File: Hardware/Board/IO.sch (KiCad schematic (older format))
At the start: 70 parts, among them U1 PCF8574A, U2 PCF8574A, U3 TJA1029T, U4 TJA1029T, U5 TJA1029T, U6 TJA1049T-3, U7 MAX3072E

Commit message: MCU Section fertig, Analog Inputs angelegt, Schaltplan neu organisiert, alte Datenblätter entfernt.
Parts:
- removed U?: MAX11613, Package_SO:MSOP-8_3x3mm_P0.65mm, symbol Analog_ADC:MAX11613
- added U?: MAX11615, Package_SO:QSOP-16_3.9x4.9mm_P0.635mm, symbol Analog_ADC:MAX11615
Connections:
- net labels added: AIN4, AIN5, AIN6, AIN7, P0, P1, P2, P3, P4, P5, P6, P7
- net labels removed: I2C1_SCL, I2C1_SDA
- wire segments 273 -> 277
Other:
- note added: "I2C ADR: 0011000"
- note added: "I2C-ADR: 0110011"
- note removed: "I2C-ADR: 0110100"
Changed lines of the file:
@@
 $Descr A3 16535 11693
 encoding utf-8
-Sheet 2 7
+Sheet 2 6
 Title ""
 Date ""
@@
 Wire Wire Line
 	13000 5100 12850 5100
-Text GLabel 11750 7500 0    50   BiDi ~ 0
+Text GLabel 11750 7900 0    50   BiDi ~ 0
 I2C2_SDA
-Text GLabel 11750 7400 0    50   Input ~ 0
+Text GLabel 11750 7800 0    50   Input ~ 0
 I2C2_SCL
 Wire Wire Line
@@
 Wire Wire Line
 	11850 4400 11750 4400
-$Comp
-L Analog_ADC:MAX11613 U?
-U 1 1 5D89986D
-P 12350 7500
-F 0 "U?" H 12800 8000 50  0000 C CNN
-F 1 "MAX11613" H 12700 7900 50  0000 C CNN
-F 2 "Package_SO:MSOP-8_3x3mm_P0.65mm" H 12800 7150 50  0001 L CNN
-F 3 "https://datasheets.maximintegrated.com/en/ds/MAX11612-MAX11617.pdf" H 12450 8000 50  0001 C CNN
-	1    12350 7500
-	-1   0    0    -1
-$EndComp
 $Comp
 L power:GND #PWR?
@@
 	0    1    1    0
 $EndComp
-$Comp
-L power:GND #PWR?
-U 1 1 5D8DBE2A
-P 12350 8100
-F 0 "#PWR?" H 12350 7850 50  0001 C CNN
-F 1 "GND" H 12355 7927 50  0000 C CNN
-F 2 "" H 12350 8100 50  0001 C CNN
-F 3 "" H 12350 8100 50  0001 C CNN
-	1    12350 8100
-	1    0    0    -1
-$EndComp
 Wire Wire Line
 	12350 6750 12350 6850
@@
 Wire Wire Line
 	12350 6850 12350 7100
-Wire Wire Line
-	11850 7400 11750 7400
-Wire Wire Line
-	11850 7500 11750 7500
-Wire Wire Line
-	12350 8000 12350 8100
-Text Notes 11450 8050 0    50   ~ 0
-I2C-ADR: 0110100
+Text Notes 11450 8650 0    50   ~ 0
+I2C-ADR: 0110011
 Text Notes 11500 3050 0    50   ~ 0
 I2C ADR: 0111001
@@
 $EndComp
 Text GLabel 6000 8150 2    50   BiDi ~ 0
-I2C1_SDA
+I2C2_SDA
 Text GLabel 6000 9150 2    50   Input ~ 0
-I2C1_SCL
+I2C2_SCL
 $Comp
 L power:+3.3VA #PWR?
@@
 Wire Wire Line
 	9750 8250 9550 8250
+Text Notes 4650 9650 0    50   ~ 0
+I2C ADR: 0011000
+$Comp
+L Analog_ADC:MAX11615 U?
+U 1 1 5F61F3FA
+P 12350 7800
+F 0 "U?" H 12750 8600 50  0000 C CNN
+F 1 "MAX11615" H 12700 8500 50  0000 C CNN
+F 2 "Package_SO:QSOP-16_3.9x4.9mm_P0.635mm" H 12800 7150 50  0001 L CNN
+F 3 "https://datasheets.maximintegrated.com/en/ds/MAX11612-MAX11617.pdf" H 12450 8600 50  0001 C CNN
+	1    12350 7800
+	-1   0    0    -1
+$EndComp
+Text GLabel 12950 7700 2    50   Input ~ 0
+AIN4
+Text GLabel 12950 7800 2    50   Input ~ 0
+AIN5
+Text GLabel 12950 7900 2    50   Input ~ 0
+AIN6
+Text GLabel 12950 8000 2    50   Input ~ 0
+AIN7
+Wire Wire Line
+	11750 7800 11850 7800
+Wire Wire Line
+	11850 7900 11750 7900
+Wire Wire Line
+	12950 7700 12850 7700
+Wire Wire Line
+	12950 7800 12850 7800
+Wire Wire Line
+	12950 7900 12850 7900
+Wire Wire Line
+	12950 8000 12850 8000
+$Comp
+L power:GND #PWR?
+U 1 1 5F70EB36
+P 12350 8700
+F 0 "#PWR?" H 12350 8450 50  0001 C CNN
+F 1 "GND" H 12355 8527 50  0000 C CNN
+F 2 "" H 12350 8700 50  0001 C CNN
+F 3 "" H 12350 8700 50  0001 C CNN
+	1    12350 8700
+	1    0    0    -1
+$EndComp
+Wire Wire Line
+	12350 8600 12350 8700
+Text GLabel 13000 4400 2    50   BiDi ~ 0
+P0
+Text GLabel 13000 4500 2    50   BiDi ~ 0
+P1
+Text GLabel 13000 4600 2    50   BiDi ~ 0
+P2
+Text GLabel 13000 4700 2    50   BiDi ~ 0
+P3
+Text GLabel 13000 4800 2    50   BiDi ~ 0
+P4
+Text GLabel 13000 4900 2    50   BiDi ~ 0
+P5
+Text GLabel 13000 5000 2    50   BiDi ~ 0
+P6
+Text GLabel 13000 5100 2    50   BiDi ~ 0
+P7
 $EndSCHEMATC

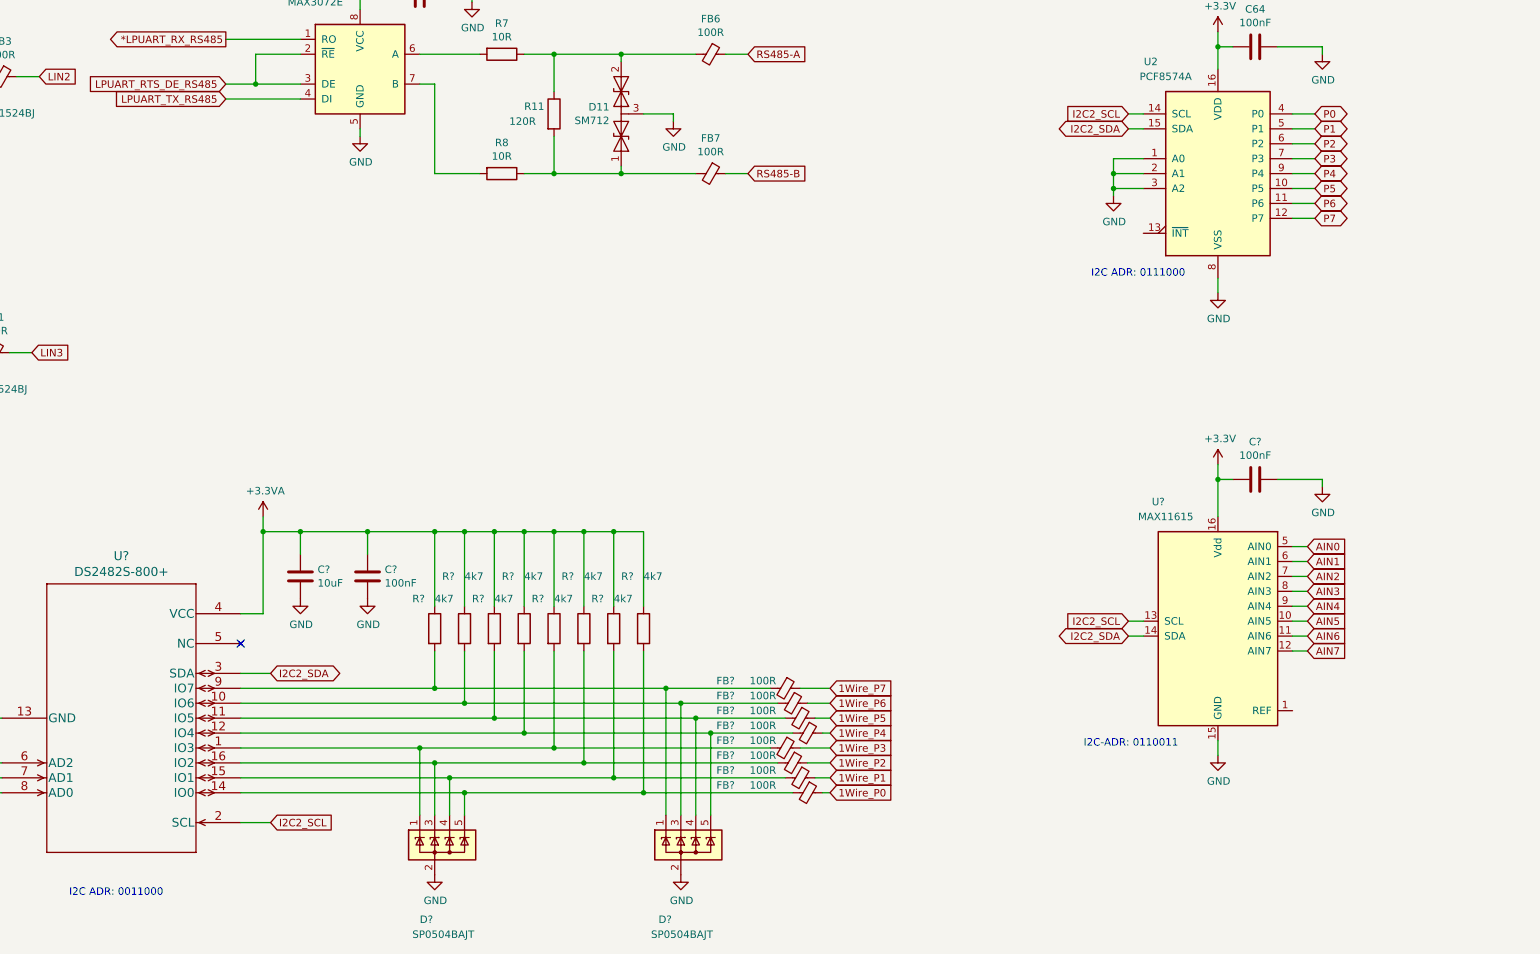
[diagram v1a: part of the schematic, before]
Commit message: Trennung MCU und Rest, Footprints fast alles zugewiesen, GSM Modul integriert, viel Kleinkram
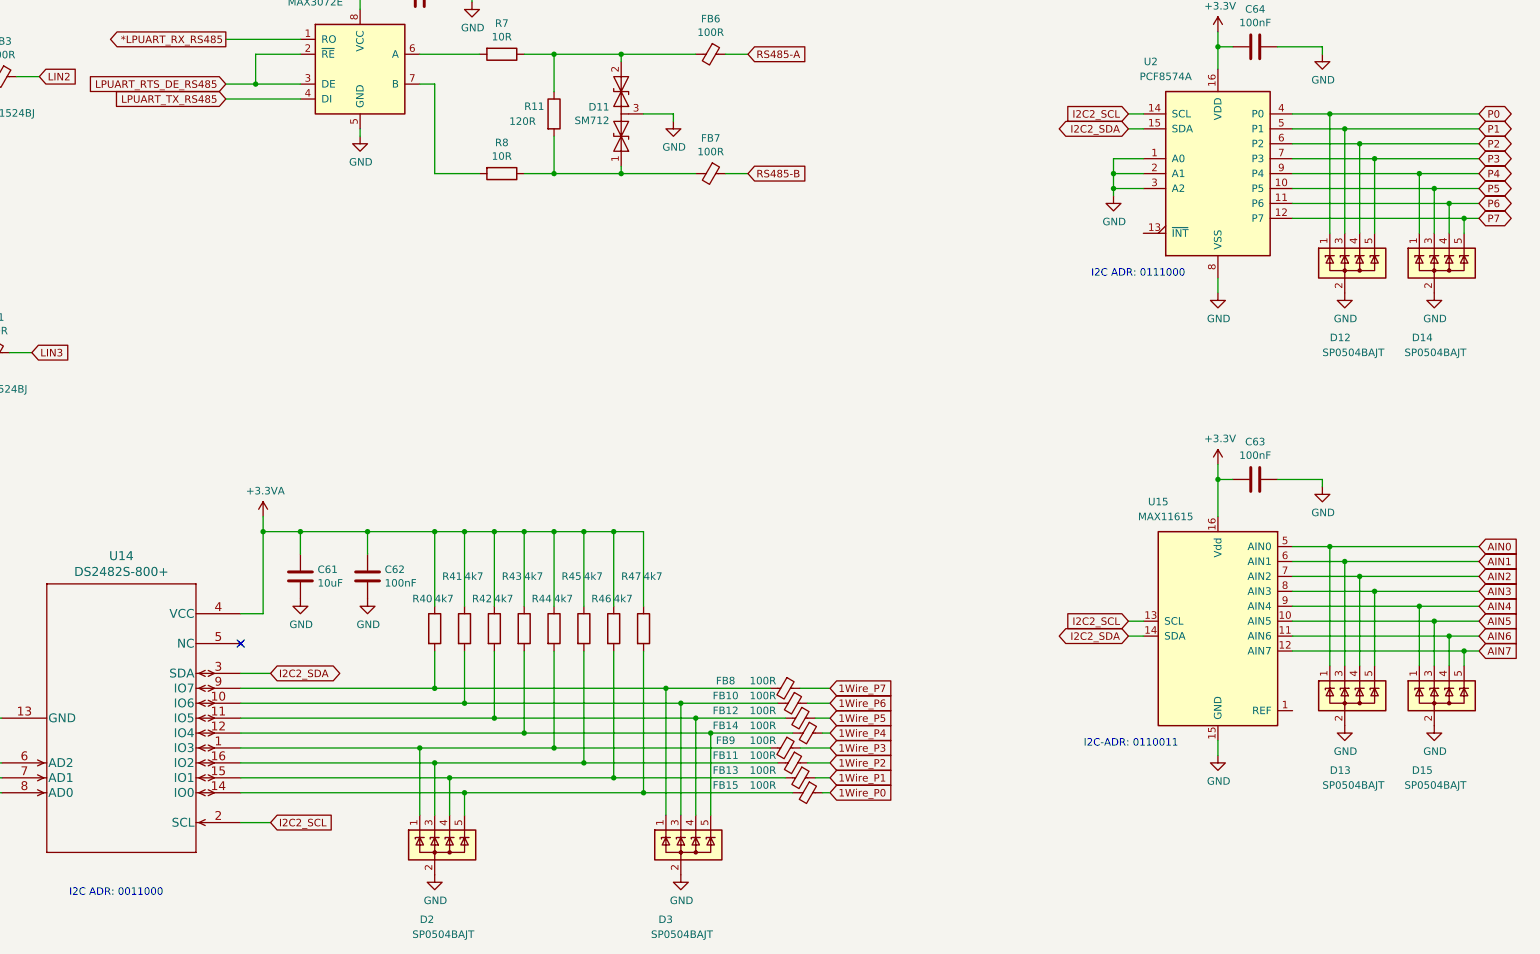
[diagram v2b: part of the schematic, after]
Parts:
- added D12, D13, D14, D15: SP0504BAJT, Package_TO_SOT_SMD:SOT-353_SC-70-5, symbol Power_Protection:SP0504BAJT
- U1, U2: footprint (none) -> Package_SO:SOIC-16W_7.5x10.3mm_P1.27mm
- gave numbers to parts that had none: 23
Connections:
- net AIN0: now also D13.1 (K)
- net AIN1: now also D13.3 (K)
- net AIN2: now also D13.4 (K)
- net AIN3: now also D13.5 (K)
- net AIN4: now also D15.1 (K)
- net AIN5: now also D15.3 (K)
- net AIN6: now also D15.4 (K)
- net AIN7: now also D15.5 (K)
- net GND: now also D12.2 (A), D13.2 (A), D14.2 (A), D15.2 (A)
- net P0: now also D12.1 (K)
- net P1: now also D12.3 (K)
- net P2: now also D12.4 (K)
- net P3: now also D12.5 (K)
- net P4: now also D14.1 (K)
- net P5: now also D14.3 (K)
- net P6: now also D14.4 (K)
- net P7: now also D14.5 (K)

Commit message: Alle Footprints definiert, Libs angepasst, Layout gestartet mit Plazierung, Controller und Breakout Netzmäßig getrennt.
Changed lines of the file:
@@
 $EndComp
-Wire Wire Line
-	12350 6750 12350 6850
-Wire Wire Line
-	12450 6850 12350 6850
-Connection ~ 12350 6850
 Wire Wire Line
 	13050 6850 13050 6900
 Wire Wire Line
 	12750 6850 13050 6850
-Wire Wire Line
-	12350 6850 12350 7100
 Text Notes 11450 8650 0    50   ~ 0
 I2C-ADR: 0110011
@@
 Wire Wire Line
 	13100 7300 14100 7300
+Wire Wire Line
+	12350 6750 12350 6850
+Wire Wire Line
+	12350 6850 12450 6850
+Wire Wire Line
+	12350 7100 12350 6850
+Connection ~ 12350 6850
 $EndSCHEMATC

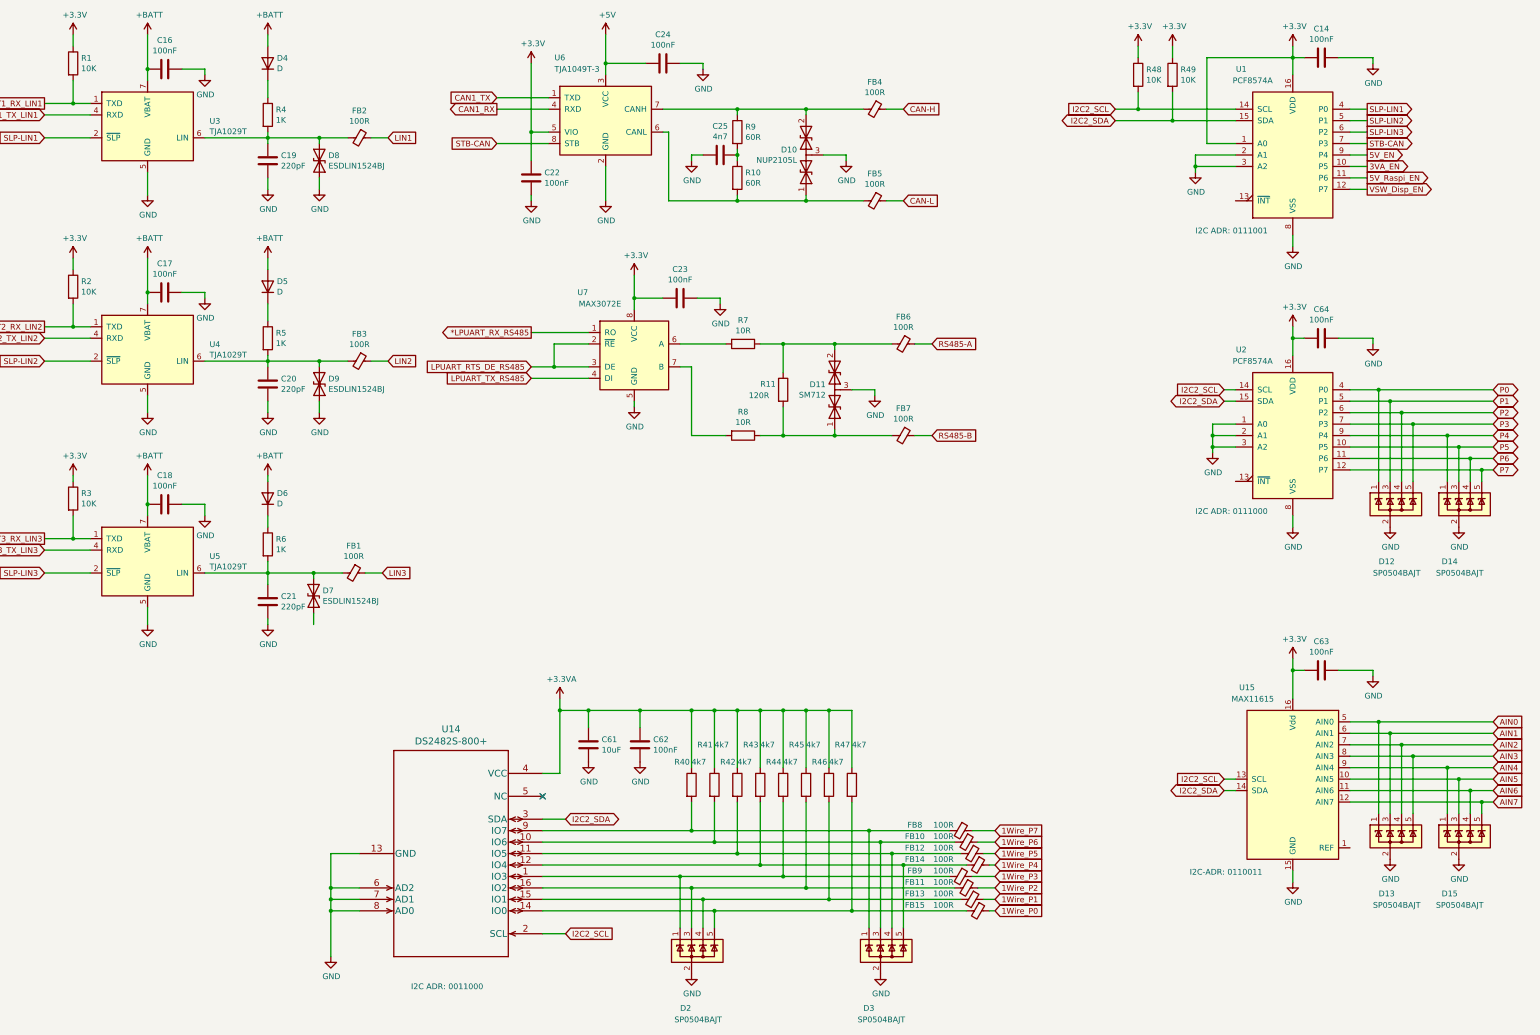
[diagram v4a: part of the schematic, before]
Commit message: Komplete enummerierung Geändert, Schaltplan zusammengefasst, Layout nochmals reset. BOM zu 75% fertig gestellt
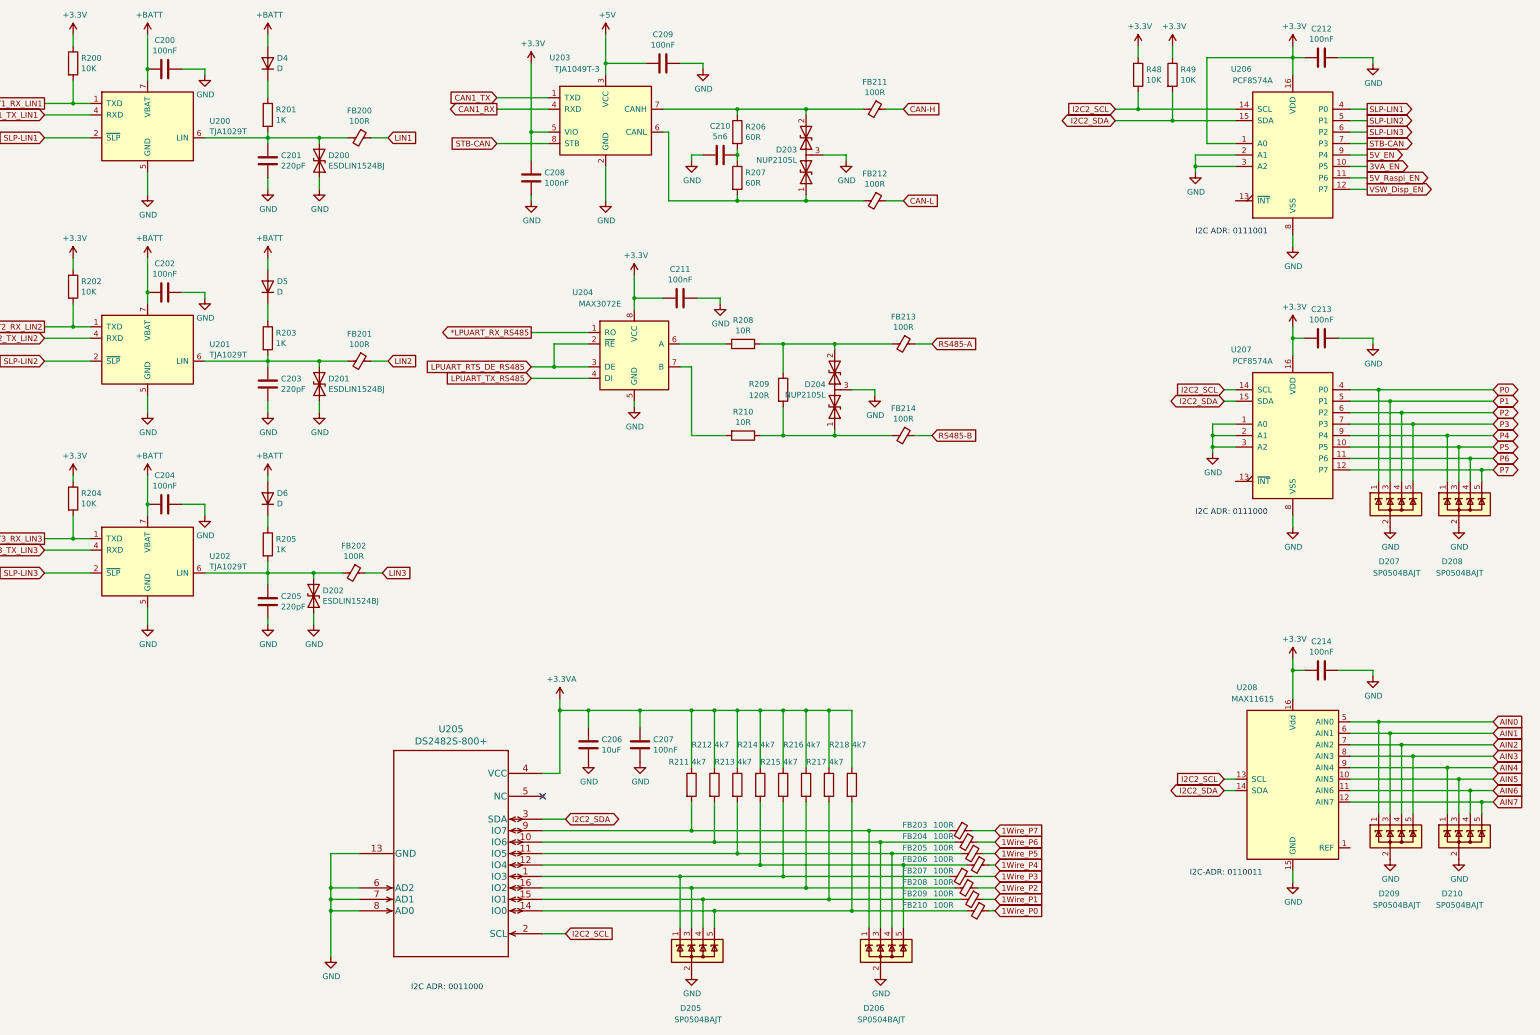
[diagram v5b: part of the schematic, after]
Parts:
- C210: renamed from C25; value 4n7 -> 5n6
- D204: renamed from D11; value SM712 -> NUP2105L
- renumbered C16 to C200, C19 to C201, C17 to C202, C20 to C203, C18 to C204, C21 to C205, C61 to C206, C62 to C207, C22 to C208, C24 to C209, C23 to C211, C14 to C212, C64 to C213, C63 to C214, D8 to D200, D9 to D201, D7 to D202, D10 to D203, D2 to D205, D3 to D206, D12 to D207, D14 to D208, D13 to D209, D15 to D210, FB2 to FB200, FB3 to FB201, FB1 to FB202, FB8 to FB203, FB10 to FB204, FB12 to FB205, FB14 to FB206, FB9 to FB207, FB11 to FB208, FB13 to FB209, FB15 to FB210, FB4 to FB211, FB5 to FB212, FB6 to FB213, FB7 to FB214, R1 to R200, R4 to R201, R2 to R202, R5 to R203, R3 to R204, R6 to R205, R9 to R206, R10 to R207, R7 to R208, R11 to R209, R8 to R210, R40 to R211, R41 to R212, R42 to R213, R43 to R214, R44 to R215, R45 to R216, R46 to R217, R47 to R218, U3 to U200, U4 to U201, U5 to U202, U6 to U203, U7 to U204, U14 to U205, U1 to U206, U2 to U207, U15 to U208
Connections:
- net GND: now also D202.2 (A2)

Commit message: Änderung des Konzeptes auf 2 Boards, eines TFT Touch mit STM32L4R9, das rein die Bedienung macht. Control Board mit STM32L476, mit noch mehr Schnittstellen. Bus zwischen Display, Board, Raspberry/ESP ist RS485, Bus als RJ45 mit Wakeup und Stromversorgung
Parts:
- added C?: 100nF, Capacitor_SMD:C_0603_1608Metric, symbol Device:C
- added C?: 220pF, Capacitor_SMD:C_0603_1608Metric, symbol Device:C
- added D?: D, Diode_SMD:D_SOD-323, symbol Device:D
- added D?: ESDLIN1524BJ, Diode_SMD:D_SOD-323, symbol Device:D_TVS
- added FB?: 100R, Inductor_SMD:L_0603_1608Metric, symbol Device:Ferrite_Bead_Small
- added R?: 1K, Resistor_SMD:R_0603_1608Metric, symbol Device:R
- added R?: 10K, Resistor_SMD:R_0603_1608Metric, symbol Device:R
- added U? (x2): 4052, symbol 4xxx_IEEE:4052
- added U?: TJA1029T, Package_SO:SOIC-8_3.9x4.9mm_P1.27mm, symbol Interface_CAN_LIN:TJA1029T
- added U? (x2): Si8642BB-B-IS1, Package_SO:SOIC-16_3.9x9.9mm_P1.27mm, symbol Isolator:Si8642BB-B-IS1
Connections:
- net +3V3: now also R?.1
- net +BATT: now also C?.2, D?.2 (A), U?.7 (VBAT)
- net GND: now also C?.1, C?.2, D?.2 (A2), U?.5 (GND)
- net USART1_RX_LIN1 renamed RX_LIN1
- net RX_LIN1: now also U?.12 (X0)
- net USART1_TX_LIN1 renamed TX_LIN1
- net TX_LIN1: now also U?.1 (Y0)
- net USART2_RX_LIN2 renamed RX_LIN2
- net RX_LIN2: now also U?.14 (X1)
- net USART2_TX_LIN2 renamed TX_LIN2
- net TX_LIN2: now also U?.5 (Y1)
- net USART3_RX_LIN3 renamed RX_LIN3
- net RX_LIN3: now also U?.15 (X2)
- net USART3_TX_LIN3 renamed TX_LIN3
- net TX_LIN3: now also U?.2 (Y2)
- new net: C?.1, D?.1 (A1), FB?.2, R?.2, U?.6 (LIN)
- new net: D?.1 (K), R?.1
- new net: U?.15 (GND2), U?.9 (GND2) (x2)
- new net: U?.2 (GND1), U?.8 (GND1) (x2)
- new net LIN4: FB?.1
- new net LIN_SEL_A0: U?.10 (A0)
- new net LIN_SEL_A1: U?.9 (A1)
- new net LIN_SEL_EN: U?.6 (~E)
- new net RX_LIN4: R?.2, U?.1 (TXD), U?.11 (X3)
- new net RX_SER1: U?.12 (X0), U?.5 (A3)
- new net RX_SER2: U?.14 (X1), U?.6 (A4)
- new net RX_SER3: U?.15 (X2), U?.5 (A3)
- new net RX_SER4: U?.11 (X3), U?.6 (A4)
- new net SER_SEL_A0: U?.10 (A0)
- new net SER_SEL_A1: U?.9 (A1)
- new net SER_SEL_EN: U?.6 (~E)
- new net SLP-LIN4: U?.2 (~SLP~)
- new net TX_LIN4: U?.4 (RXD), U?.4 (Y3)
- new net TX_SER1: U?.1 (Y0), U?.3 (A1)
- new net TX_SER2: U?.4 (A2), U?.5 (Y1)
- new net TX_SER3: U?.2 (Y2), U?.3 (A1)
- new net TX_SER4: U?.4 (A2), U?.4 (Y3)
- new net USART2_RX_LIN: U?.13 (X)
- new net USART2_TX_LIN: U?.3 (Y)
- new net USART3_RX_SER: U?.13 (X)
- new net USART3_TX_SER: U?.3 (Y)
- new net VEE: U?.7 (VEE), U?.7 (VEE)
- new net Vdd: U?.16 (Vdd), U?.16 (Vdd)
- new net Vss: U?.8 (Vss), U?.8 (Vss)
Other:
- moved on the sheet: C200, C201, C202, C203, C204, C205, C206, C207, C208, C209, C210, C211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
